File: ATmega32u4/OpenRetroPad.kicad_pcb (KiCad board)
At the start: 4 copper layers, 46 x 74 mm, 68 parts, among them J1 USB_C_Receptacle_USB2.0, J2 USB_C_Receptacle_USB2.0, J3 NRF24, J4 DB25_Male_MountingHoles, SW1 HWB, SW2 RESET, U1 AMS1117-3.3, U2 ATmega32U4-M, U3 CH330N, U4 USBLC6-2SC6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

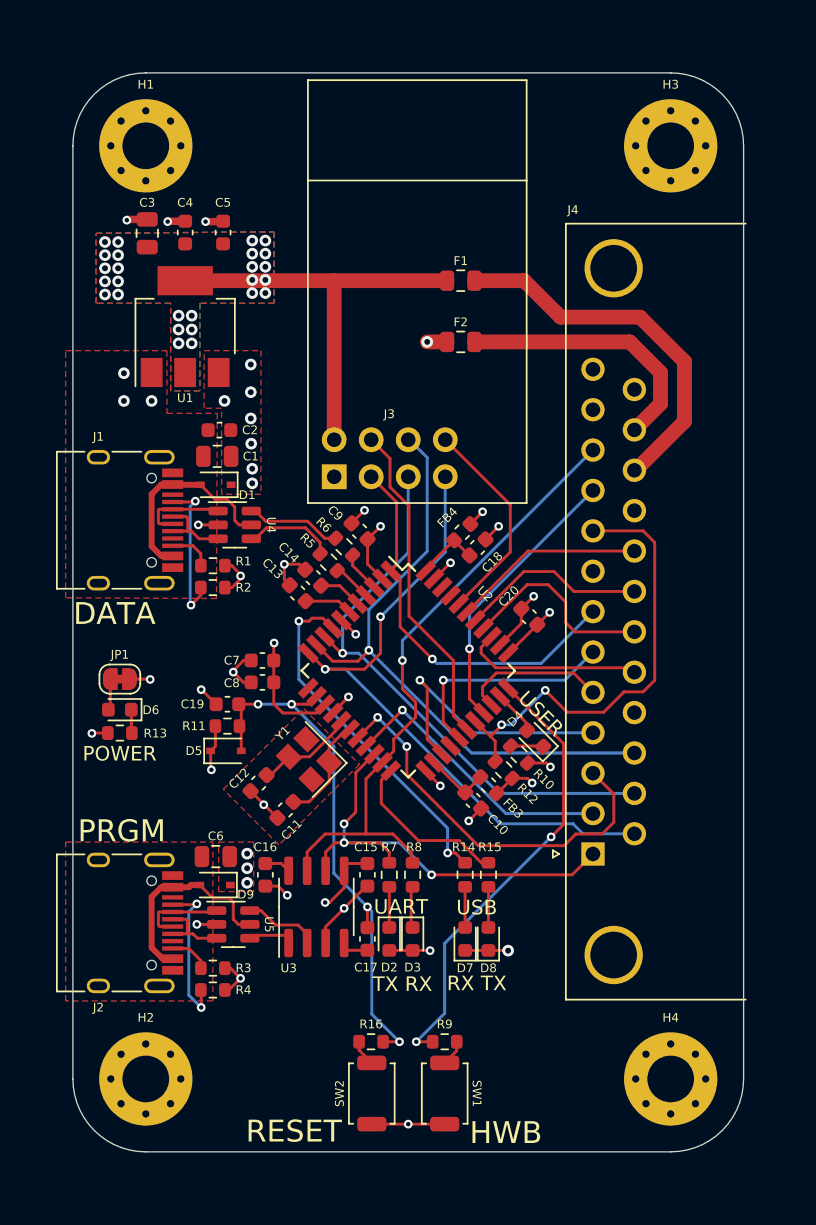
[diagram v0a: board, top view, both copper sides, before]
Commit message: Schematic, routing and layout changes post review.
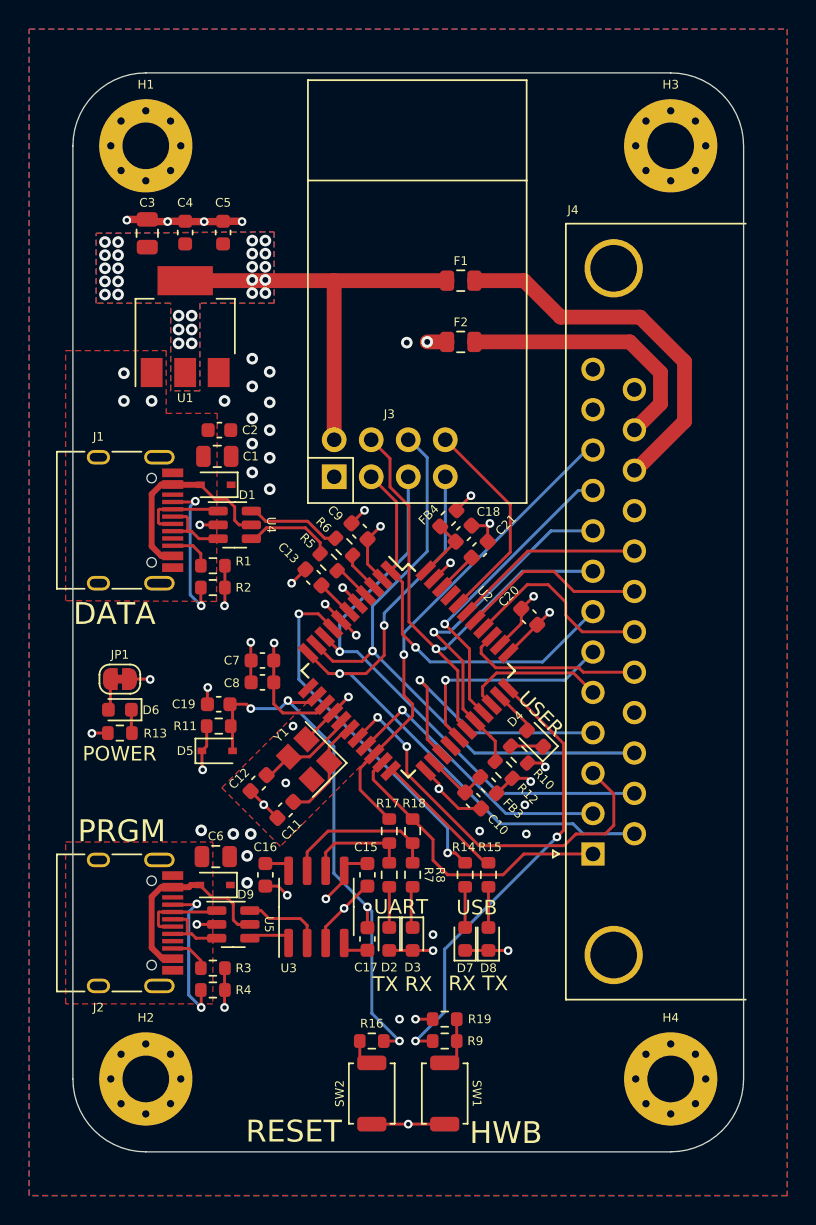
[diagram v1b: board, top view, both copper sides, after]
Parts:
- removed C14: 1u, Capacitor_SMD:C_0603_1608Metric
- added C21: 100n, Capacitor_SMD:C_0603_1608Metric, F.Cu at (92.9, 97.7)
- added R17: 1k, Resistor_SMD:R_0603_1608Metric, F.Cu at (86.7, 117.0)
- added R18: 1k, Resistor_SMD:R_0603_1608Metric, F.Cu at (88.3, 117.0)
- added R19: 10k, Resistor_SMD:R_0603_1608Metric, F.Cu at (90.5, 129.9)
- moved C13 1.53 mm to (81.5, 99.6)
- moved C18 1.34 mm to (91.8, 96.6)
- moved FB4 1.34 mm to (90.7, 95.6)
- moved C19 0.60 mm to (75.0, 108.3)
- moved D5 0.60 mm to (74.9, 111.5)
- moved R11 0.60 mm to (75.0, 109.8)
- moved R16 0.07 mm to (85.5, 131.4)
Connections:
- net /DB25/CE renamed /DB25/PE6-CE
- net /DB25/IRQ renamed /DB25/PF1-IRQ
- net /DB25/MISO renamed /DB25/PB3-MISO
- net /DB25/MOSI renamed /DB25/PB2-MOSI
- net /DB25/SCK renamed /DB25/PB1-SCK
- net /IO/LED_USER renamed /PC7-LED_USER
- net /IO/RX_LED renamed /PB0-RX_LED
- net /IO/SW_HWB renamed /PE2-HWB
- net /IO/TX_LED renamed /PD5-TX_LED
- J3 pad 4: /DB25/CSN -> /DB25/PB4-CSN
- J4 pad 1: /DB25/TX -> /DB25/PD3-TX
- J4 pad 11: /DB25/RX -> /DB25/PD2-RX
- J4 pad 8: /DB25/PB4 -> /DB25/PB4-CSN
- R7 pad 2: /DB25/TX -> /UART/TXD
- R8 pad 2: /DB25/RX -> /UART/RXD
- U2 pad 20: /DB25/TX -> /DB25/PD2-RX
- U2 pad 21: /DB25/RX -> /DB25/PD3-TX
- U2 pad 28: /DB25/CSN -> /DB25/PB4-CSN
- U2 pad 42: unconnected-(U2-Pad42) -> /Microcontroller/AREF
- U2 pad 5: /Microcontroller/UGND -> GND
- U3 pad 6: /DB25/TX -> /UART/TXD
- U3 pad 7: /DB25/RX -> /UART/RXD
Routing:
- net /DB25/RX: track 43.7 -> 0.00 mm, vias 1 -> 0
- net /DB25/PB4-CSN: track 0.00 -> 35.6 mm, vias 0 -> 1
- net /DB25/PD2-RX: track 0.00 -> 33.5 mm, vias 0 -> 1
- net /DB25/TX: track 32.4 -> 0.00 mm, vias 3 -> 0
- net /DB25/CSN: track 22.6 -> 0.00 mm
- net /DB25/PD3-TX: track 0.00 -> 20.6 mm
- net /UART/RXD: track 0.00 -> 10.8 mm
- net GND: track 52.9 -> 61.6 mm, vias 27 -> 40
- net /UART/TXD: track 0.00 -> 7.24 mm
- net /DB25/PB5: track 31.5 -> 24.4 mm, vias 2 -> 1
- net /Microcontroller/UGND: track 3.02 -> 0.00 mm
- net /Microcontroller/AREF: track 0.00 -> 2.86 mm
- net +5V: track 35.9 -> 38.5 mm, vias 21 -> 25
- net /PD5-TX_LED: track 11.5 -> 9.32 mm
- net Net-(R19-Pad2): track 1.79 -> 3.83 mm
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- added copper zone on B.Cu, net +5V
- added copper zone on In2.Cu, net GND
- removed copper zone on In2.Cu, net +5V
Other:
- board text added: "3V3"
- board text added: "CE"
- board text added: "CSN"
- board text added: "DB25 --- 13 25 12 24 11 23 10 22 9 21 8 20 7 19 6 18 5 17 4 16 3 15 2 14 1"
- board text added: "GND"
- board text added: "GPIO --- - - - - D0,RX - D10 - D9 D21,A3 D8 D20,A2 D7 D19,A1 D6,A7 D18,A0 D5 - D4,A6 D16 D3,SCL D15 D2,SDA D14 D1,TX"
- board text added: "IRQ"
- board text added: "MCU --- - GND - 5V PD2 3V3 PB6 - PB5 PF4 PB4 PF5 PE6 PF6 PD7 PF7 PC6 - PD4 PB2 PD0 PB1 PD1 PB3 PD3"
- board text added: "MISO"
- board text added: "MOSI"
- board text added: "OpenRetroPad ATmega32u4 v2 DEC-2022 OpenRetroPad.com"
- board text added: "SCK"
- board text removed: "OpenRetroPad ATmega32u4 v2 DEC-2022 OpenRetroPad.com JLCJLCJLCJLC"

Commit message: Update notes, add io for reading cc pins, minor changes to schematic and routing.
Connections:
- J1 pad A5: /USB Data/CC1 -> /PB7-CC1
- J1 pad B5: /USB Data/CC2 -> /PD6-CC2
- R1 pad 1: /USB Data/CC2 -> /PD6-CC2
- R2 pad 2: /USB Data/CC1 -> /PB7-CC1
- U2 pad 12: unconnected-(U2-Pad12) -> /PB7-CC1
- U2 pad 26: unconnected-(U2-Pad26) -> /PD6-CC2
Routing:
- net /PD6-CC2: track 0.00 -> 30.2 mm
- net /PB7-CC1: track 0.00 -> 21.3 mm, vias 0 -> 2
- net /USB Data/CC1: track 10.5 -> 0.00 mm, vias 2 -> 0
- net /USB Data/CC2: track 2.98 -> 0.00 mm
- net /DB25/PD4: track 19.1 -> 21.2 mm
- net +5V: track 38.5 -> 37.1 mm, vias 25 -> 24
- net /DB25/PD2-RX: track 33.5 -> 34.6 mm
- net /DB25/PB2-MOSI: track 42.0 -> 43.0 mm
- net /DB25/PB3-MISO: track 45.1 -> 44.1 mm
- net GND: track 61.6 -> 61.5 mm, vias 40 -> 46

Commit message: Adjust copper pours on top/bottom layers, update assembly pdf to include inner layers
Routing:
- net +5V: track 37.1 -> 35.7 mm, vias 24 -> 22
- net GND: vias 46 -> 48
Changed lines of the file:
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@@
   (via (at 77.225 104.075) (size 0.6) (drill 0.3) (layers "F.Cu" "B.Cu") (net 1))
   (via (at 83.6 122.3) (size 0.6) (drill 0.3) (layers "F.Cu" "B.Cu") (net 1))
+  (via (at 73 112.8) (size 0.6) (drill 0.3) (layers "F.Cu" "B.Cu") (free) (net 1))
   (via (at 68.7 75.1) (size 0.6) (drill 0.3) (layers "F.Cu" "B.Cu") (net 1))
-  (via (at 77.2 117.2) (size 0.8) (drill 0.4) (layers "F.Cu" "B.Cu") (free) (net 1))
+  (via (at 77.2 117.3) (size 0.8) (drill 0.4) (layers "F.Cu" "B.Cu") (free) (net 1))
   (via (at 70.4 87.5) (size 0.8) (drill 0.4) (layers "F.Cu" "B.Cu") (free) (net 1))
   (via (at 96.6 100.9) (size 0.6) (drill 0.3) (layers "F.Cu" "B.Cu") (net 1))
@@
   (via (at 78.5 91.4) (size 0.8) (drill 0.4) (layers "F.Cu" "B.Cu") (free) (net 1))
   (via (at 74.25 107.15) (size 0.6) (drill 0.3) (layers "F.Cu" "B.Cu") (net 1))
+  (via (at 94.1 117.3) (size 0.6) (drill 0.3) (layers "F.Cu" "B.Cu") (free) (net 1))
   (via (at 93.6 95.9) (size 0.6) (drill 0.3) (layers "F.Cu" "B.Cu") (net 1))
   (via (at 85 95) (size 0.6) (drill 0.3) (layers "F.Cu" "B.Cu") (net 1))
@@
   (segment (start 78.775 105.3) (end 78.775 106.8) (width 0.2032) (layer "F.Cu") (net 2))
   (segment (start 78.775 105.3) (end 78.775 104.125) (width 0.2032) (layer "F.Cu") (net 2))
-  (segment (start 96.183363 113.383363) (end 95.133363 113.383363) (width 0.2032) (layer "F.Cu") (net 2))
   (segment (start 83.605 119.225) (end 83.605 119.725) (width 0.2032) (layer "F.Cu") (net 2))
-  (segment (start 94.109879 114.406847) (end 95.133363 113.383363) (width 0.2032) (layer "F.Cu") (net 2))
   (segment (start 74.175 109.8) (end 74.175 111.175) (width 0.2032) (layer "F.Cu") (net 2))
   (segment (start 70.276 106.576) (end 70.3 106.6) (width 0.2032) (layer "F.Cu") (net 2))
   (segment (start 94.898098 104.797918) (end 96.848008 102.848008) (width 0.2032) (layer "F.Cu") (net 2))
+  (segment (start 94.109879 114.406847) (end 95.133363 113.383363) (width 0.2032) (layer "F.Cu") (net 2))
   (segment (start 82.35 121.65) (end 83.605 120.395) (width 0.2032) (layer "F.Cu") (net 2))
   (segment (start 81.705887 108.9) (end 79.4 108.9) (width 0.2032) (layer "F.Cu") (net 2))
@@
   (segment (start 85.208668 96.987348) (end 85.208668 98.683185) (width 0.2032) (layer "F.Cu") (net 2))
   (segment (start 91.304855 94.995145) (end 92.3 94) (width 0.2032) (layer "F.Cu") (net 2))
+  (segment (start 94.056847 114.406847) (end 94.109879 114.406847) (width 0.2032) (layer "F.Cu") (net 2))
   (segment (start 85.212652 96.987348) (end 86.1 96.1) (width 0.2032) (layer "F.Cu") (net 2))
   (segment (start 73.85 111.5) (end 73.85 112.75) (width 0.2032) (layer "F.Cu") (net 2))
   (segment (start 89.675 129.9) (end 88.5 129.9) (width 0.2032) (layer "F.Cu") (net 2))
-  (segment (start 94.056847 114.406847) (end 94.109879 114.406847) (width 0.2032) (layer "F.Cu") (net 2))
   (segment (start 83.605 120.395) (end 83.605 119.725) (width 0.2032) (layer "F.Cu") (net 2))
   (segment (start 74.175 111.175) (end 73.85 111.5) (width 0.2032) (layer "F.Cu") (net 2))
@@
   (segment (start 90.6625 83.45) (end 89.3 83.45) (width 1.016) (layer "F.Cu") (net 2))
   (segment (start 73.85 112.75) (end 73.9 112.8) (width 0.2032) (layer "F.Cu") (net 2))
-  (segment (start 96.4 113.6) (end 96.183363 113.383363) (width 0.2032) (layer "F.Cu") (net 2))
   (segment (start 82.3 101.431371) (end 83.403806 102.535177) (width 0.2032) (layer "F.Cu") (net 2))
   (via (at 82.35 121.65) (size 0.6) (drill 0.3) (layers "F.Cu" "B.Cu") (net 2))
@@
   (via (at 73.9 112.8) (size 0.6) (drill 0.3) (layers "F.Cu" "B.Cu") (net 2))
   (via (at 89.7 125.2) (size 0.6) (drill 0.3) (layers "F.Cu" "B.Cu") (net 2))
-  (via (at 96 115.2) (size 0.6) (drill 0.3) (layers "F.Cu" "B.Cu") (free) (net 2))
   (via (at 77.3 90.43) (size 0.8) (drill 0.4) (layers "F.Cu" "B.Cu") (free) (net 2))
   (via (at 76.95 118.7) (size 0.8) (drill 0.4) (layers "F.Cu" "B.Cu") (free) (net 2))
@@
   (via (at 92.3 94) (size 0.6) (drill 0.3) (layers "F.Cu" "B.Cu") (net 2))
   (via (at 77.3 86.5) (size 0.8) (drill 0.4) (layers "F.Cu" "B.Cu") (free) (net 2))
-  (via (at 96.4 113.6) (size 0.6) (drill 0.3) (layers "F.Cu" "B.Cu") (net 2))
   (via (at 97.7 102) (size 0.6) (drill 0.3) (layers "F.Cu" "B.Cu") (net 2))
   (via (at 89.3 83.45) (size 0.8) (drill 0.4) (layers "F.Cu" "B.Cu") (net 2))

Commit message: Change CC pin <-> ADC pin, adjust routing
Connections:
- J1 pad A5: /PB7-CC1 -> /PF0-CC1
- R2 pad 2: /PB7-CC1 -> /PF0-CC1
- U2 pad 12: /PB7-CC1 -> unconnected-(U2-Pad12)
- U2 pad 41: unconnected-(U2-Pad41) -> /PF0-CC1
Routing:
- net /PF0-CC1: track 0.00 -> 46.7 mm, vias 0 -> 3
- net /PB7-CC1: track 21.3 -> 0.00 mm, vias 2 -> 0
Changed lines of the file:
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@@
   (net 28 "/DB25/PB6")
   (net 29 "/DB25/PD0")
-  (net 30 "/PB7-CC1")
+  (net 30 "/PF0-CC1")
   (net 31 "/DB25/PD4")
   (net 32 "/DB25/PB5")
@@
   (net 46 "unconnected-(J4-Pad17)")
   (net 47 "unconnected-(J4-Pad22)")
-  (net 48 "unconnected-(U2-Pad41)")
+  (net 48 "unconnected-(U2-Pad12)")
   (net 49 "/USB Data/VBUS")
   (net 50 "/USB Program/VBUS")
@@
       (net 1 "GND") (pintype "passive"))
     (pad "2" smd roundrect (at 0.825 0 180) (size 0.8 0.95) (layers "F.Cu" "F.Paste" "F.Mask") (roundrect_rratio 0.25)
-      (net 30 "/PB7-CC1") (pintype "passive"))
+      (net 30 "/PF0-CC1") (pintype "passive"))
     (model "${KICAD6_3DMODEL_DIR}/Resistor_SMD.3dshapes/R_0603_1608Metric.wrl"
       (offset (xyz 0 0 0))
@@
       (net 49 "/USB Data/VBUS") (pinfunction "VBUS") (pintype "passive"))
     (pad "A5" smd rect (at -1.25 -4.045 270) (size 0.3 1.45) (layers "F.Cu" "F.Paste" "F.Mask")
-      (net 30 "/PB7-CC1") (pinfunction "CC1") (pintype "bidirectional"))
+      (net 30 "/PF0-CC1") (pinfunction "CC1") (pintype "bidirectional"))
     (pad "A6" smd rect (at -0.25 -4.045 270) (size 0.3 1.45) (layers "F.Cu" "F.Paste" "F.Mask")
       (net 60 "/USB Data/D+") (pinfunction "D+") (pintype "bidirectional"))
@@
       (net 70 "/DB25/PB3-MISO") (pinfunction "PB3") (pintype "bidirectional"))
     (pad "12" smd rect (at -4 5.7 45) (size 1.5 0.55) (layers "F.Cu" "F.Paste" "F.Mask")
-      (net 30 "/PB7-CC1") (pinfunction "PB7") (pintype "bidirectional"))
+      (net 48 "unconnected-(U2-Pad12)") (pinfunction "PB7") (pintype "bidirectional+no_connect"))
     (pad "13" smd rect (at -3.2 5.7 45) (size 1.5 0.55) (layers "F.Cu" "F.Paste" "F.Mask")
       (net 4 "/DB25/RST") (pinfunction "~{RESET}") (pintype "input"))
@@
       (net 71 "/DB25/PF1-IRQ") (pinfunction "PF1") (pintype "bidirectional"))
     (pad "41" smd rect (at -1.6 -5.7 45) (size 1.5 0.55) (layers "F.Cu" "F.Paste" "F.Mask")
-      (net 48 "unconnected-(U2-Pad41)") (pinfunction "PF0") (pintype "bidirectional+no_connect"))
+      (net 30 "/PF0-CC1") (pinfunction "PF0") (pintype "bidirectional"))
     (pad "42" smd rect (at -2.4 -5.7 45) (size 1.5 0.55) (layers "F.Cu" "F.Paste" "F.Mask")
       (net 68 "/Microcontroller/AREF") (pinfunction "AREF") (pintype "passive"))
@@
   (via (at 85.9 109.2) (size 0.6) (drill 0.3) (layers "F.Cu" "B.Cu") (net 29))
   (segment (start 87.9 111.2) (end 85.9 109.2) (width 0.2032) (layer "B.Cu") (net 29))
-  (segment (start 79.7 105.761018) (end 79.7 103.75) (width 0.2032) (layer "F.Cu") (net 30))
+  (segment (start 89.3 90.7) (end 90 91.4) (width 0.2032) (layer "F.Cu") (net 30))
   (segment (start 73.3465 94.43) (end 73.4 94.3765) (width 0.2032) (layer "F.Cu") (net 30))
-  (segment (start 79.7 103.75) (end 78.5 102.55) (width 0.2032) (layer "F.Cu") (net 30))
-  (segment (start 78.5 102.55) (end 74.8 102.55) (width 0.2032) (layer "F.Cu") (net 30))
+  (segment (start 90 91.4) (end 91.1 91.4) (width 0.2032) (layer "F.Cu") (net 30))
   (segment (start 73.775 101.525) (end 73.775 100.3) (width 0.2032) (layer "F.Cu") (net 30))
-  (segment (start 74.8 102.55) (end 73.8 101.55) (width 0.2032) (layer "F.Cu") (net 30))
   (segment (start 73.8 101.55) (end 73.775 101.525) (width 0.2032) (layer "F.Cu") (net 30))
-  (segment (start 81.141064 107.202082) (end 79.7 105.761018) (width 0.2032) (layer "F.Cu") (net 30))
+  (segment (start 88.1 88.4) (end 89.3 89.6) (width 0.2032) (layer "F.Cu") (net 30))
+  (segment (start 84.2 88.4) (end 88.1 88.4) (width 0.2032) (layer "F.Cu") (net 30))
+  (segment (start 89.3 89.6) (end 89.3 90.7) (width 0.2032) (layer "F.Cu") (net 30))
+  (segment (start 91.1 91.4) (end 94.4 94.7) (width 0.2032) (layer "F.Cu") (net 30))
   (segment (start 71.845 94.43) (end 73.3465 94.43) (width 0.2032) (layer "F.Cu") (net 30))
+  (segment (start 94.4 94.7) (end 94.4 97.337258) (width 0.2032) (layer "F.Cu") (net 30))
+  (segment (start 94.4 97.337258) (end 90.899138 100.83812) (width 0.2032) (layer "F.Cu") (net 30))
   (via (at 73.8 101.55) (size 0.6) (drill 0.3) (layers "F.Cu" "B.Cu") (net 30))
+  (via (at 84.2 88.4) (size 0.6) (drill 0.3) (layers "F.Cu" "B.Cu") (net 30))
   (via (at 73.4 94.3765) (size 0.6) (drill 0.3) (layers "F.Cu" "B.Cu") (net 30))
   (segment (start 73.8 101.55) (end 73.046 100.796) (width 0.2032) (layer "B.Cu") (net 30))
+  (segment (start 84.2 88.4) (end 81.6 88.4) (width 0.2032) (layer "B.Cu") (net 30))
+  (segment (start 80.5 92.8) (end 78.9235 94.3765) (width 0.2032) (layer "B.Cu") (net 30))
+  (segment (start 80.5 89.5) (end 80.5 92.8) (width 0.2032) (layer "B.Cu") (net 30))
   (segment (start 73.046 100.796) (end 73.046 94.7305) (width 0.2032) (layer "B.Cu") (net 30))
+  (segment (start 81.6 88.4) (end 80.5 89.5) (width 0.2032) (layer "B.Cu") (net 30))
+  (segment (start 78.9235 94.3765) (end 73.4 94.3765) (width 0.2032) (layer "B.Cu") (net 30))
   (segment (start 73.046 94.7305) (end 73.4 94.3765) (width 0.2032) (layer "B.Cu") (net 30))
   (segment (start 87.55 106.4) (end 89.3 108.15) (width 0.2032) (layer "F.Cu") (net 31))
